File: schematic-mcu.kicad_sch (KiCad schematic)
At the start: 28 parts, among them U5 USBLC6-2P6, U6 ESP32-S3FN8, Y1 Crystal_GND24

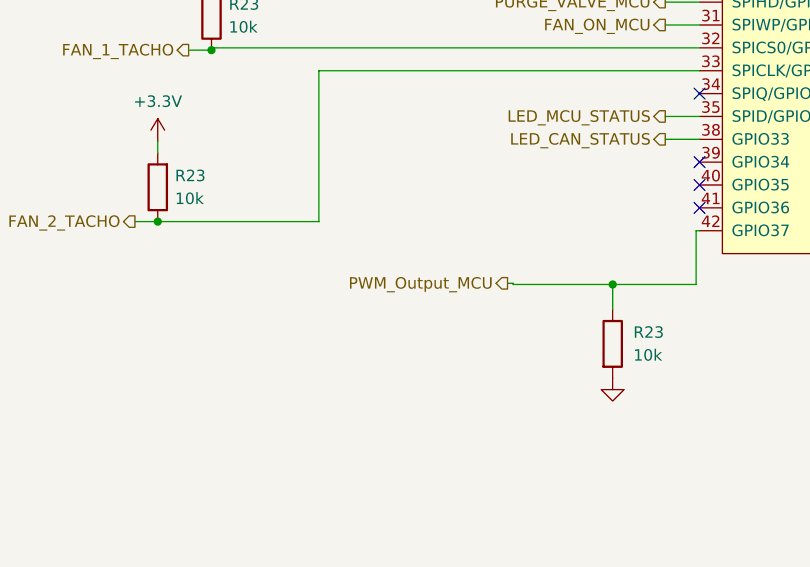
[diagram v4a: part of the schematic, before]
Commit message: Change FC connector to 10pin & ideal diode sircuit
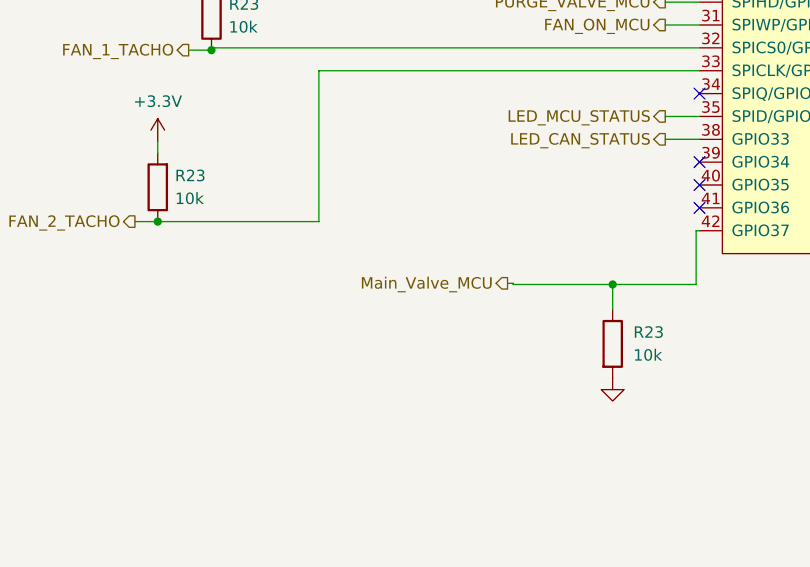
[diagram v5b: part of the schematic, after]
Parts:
- L3: footprint Inductor_SMD:LQG15WH0N7B02D -> Inductor_SMD:L_0402_1005Metric
- Y1: footprint Crystal:KC3225K400000C1GE00 -> library:KC3225K400000C1GE00
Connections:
- net PWM_Output_MCU renamed Main_Valve_MCU
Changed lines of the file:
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@@
     (effects (font (size 1.27 1.27)) (justify right))
   )
-  (hierarchical_label "PWM_Output_MCU" (shape output) (at 174.244 151.892 180) (fields_autoplaced)
+  (hierarchical_label "Main_Valve_MCU" (shape output) (at 174.244 151.892 180) (fields_autoplaced)
     (effects (font (size 1.27 1.27)) (justify right))
   )
@@
       (effects (font (size 1.27 1.27)))
     )
-    (property "Footprint" "Inductor_SMD:LQG15WH0N7B02D" (at 194.31 53.34 0)
+    (property "Footprint" "Inductor_SMD:L_0402_1005Metric" (at 194.31 53.34 0)
       (effects (font (size 1.27 1.27)) hide)
     )
@@
       (effects (font (size 1.27 1.27)) hide)
     )
-    (property "Footprint" "Crystal:KC3225K400000C1GE00" (at 59.309 159.639 0)
-      (effects (font (size 1.27 1.27)) hide)
-    )
+    (property "Footprint" "library:KC3225K400000C1GE00" (at 59.309 159.639 0)
+      (effects (font (size 1.27 1.27)) hide)
+    )

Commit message: Complate frist version
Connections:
- net FAN_1_TACHO renamed FAN_1_TACHO_MCU
- net FAN_2_TACHO renamed FAN_2_TACHO_MCU
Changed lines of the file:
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@@
     (effects (font (size 1.27 1.27)) (justify right))
   )
-  (hierarchical_label "FAN_1_TACHO" (shape output) (at 138.811 125.984 180) (fields_autoplaced)
+  (hierarchical_label "FAN_1_TACHO_MCU" (shape input) (at 138.811 125.984 180) (fields_autoplaced)
     (effects (font (size 1.27 1.27)) (justify right))
   )
@@
     (effects (font (size 1.27 1.27)) (justify right))
   )
-  (hierarchical_label "FAN_2_TACHO" (shape output) (at 132.842 145.034 180) (fields_autoplaced)
+  (hierarchical_label "FAN_2_TACHO_MCU" (shape input) (at 132.842 145.034 180) (fields_autoplaced)
     (effects (font (size 1.27 1.27)) (justify right))
   )
@@
   (symbol (lib_id "Device:C") (at 72.771 102.997 0) (unit 1)
     (in_bom yes) (on_board yes) (dnp no) (fields_autoplaced)
-    (property "Reference" "C1" (at 76.581 101.7269 0)
-      (effects (font (size 1.27 1.27)) (justify left))
-    )
-    (property "Value" "100n" (at 76.581 104.2669 0)
-      (effects (font (size 1.27 1.27)) (justify left))
-    )
+    (property "Reference" "C1" (at 76.2 101.727 0)
+      (effects (font (size 1.27 1.27)) (justify left))
+    )
+    (property "Value" "100n" (at 76.2 104.267 0)
+      (effects (font (size 1.27 1.27)) (justify left))
+    )

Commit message: New pcb 1
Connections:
- net I/O_1_MCU: now reaches U6.12 (GPIO7/ADC1_CH6)
- net I/O_2_MCU: now reaches U6.13 (GPIO8/ADC1_CH7)
- net I/O_3_MCU: now reaches U6.16 (GPIO11/ADC2_CH0)
- net I/O_4_MCU: now reaches U6.18 (GPIO13/ADC2_CH2)
- no-connect marks 30 -> 26

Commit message: Power stage pcb complate
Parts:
- renumbered C35 to C15, C4 to C16, C5 to C17, C1 to C18, C2 to C19, C2 to C20, C32 to C21, C33 to C22, C30 to C23, C31 to C24, C8 to C25, C34 to C26, C28 to C27, C29 to C28, R5 to R16, R23 to R17, R23 to R18, R23 to R19, R23 to R20, R23 to R21, R23 to R22, U5 to U3, U6 to U4
